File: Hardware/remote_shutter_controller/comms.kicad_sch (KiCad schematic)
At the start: 9 parts

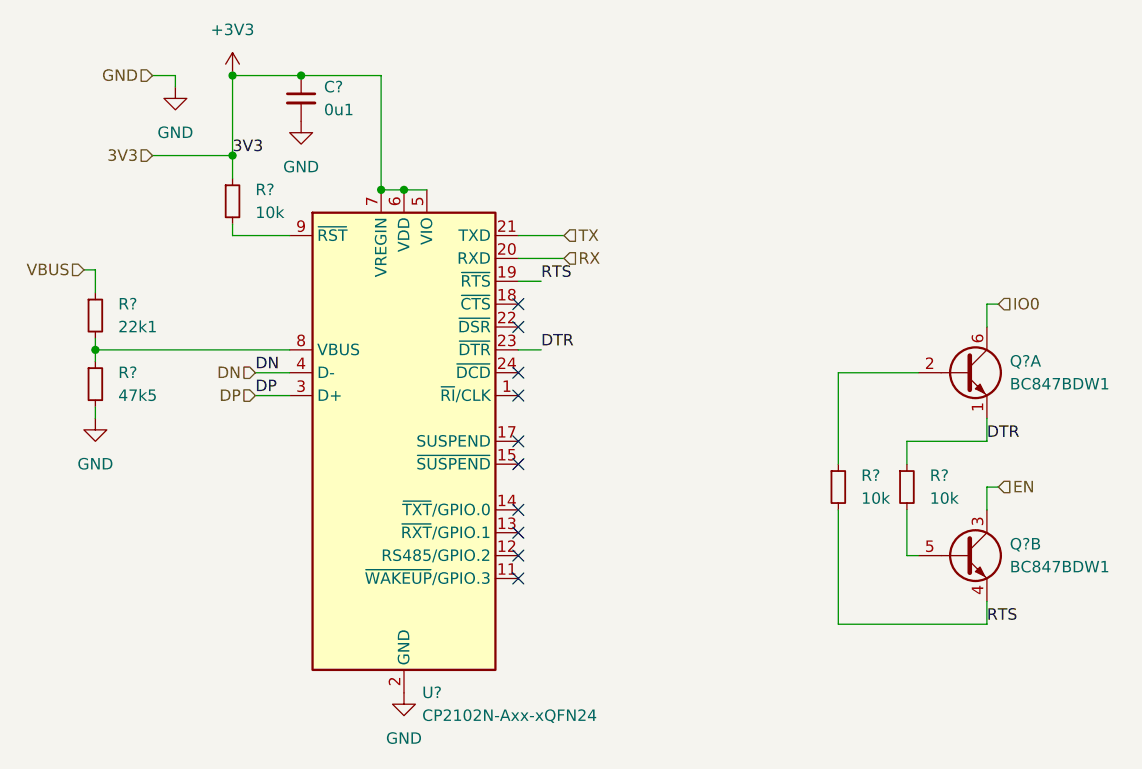
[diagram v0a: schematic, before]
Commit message: Schematic updates. First export to PCB
Added 9V line, OLED switch circuit. Added OLED footprint.
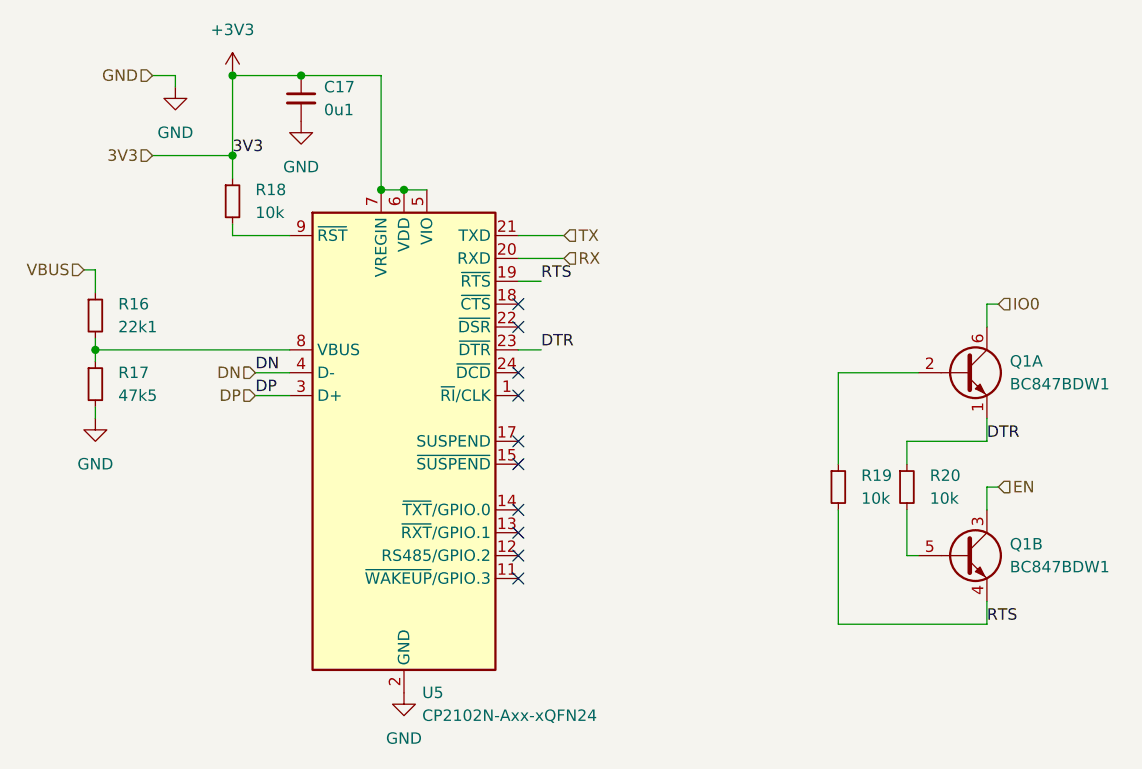
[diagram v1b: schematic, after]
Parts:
- gave numbers to parts that had none: 8
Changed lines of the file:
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@@
   (symbol (lib_id "power:GND") (at 95.25 97.79 0) (unit 1)
     (in_bom yes) (on_board yes) (fields_autoplaced)
-    (property "Reference" "#PWR?" (id 0) (at 95.25 104.14 0)
+    (property "Reference" "#PWR033" (id 0) (at 95.25 104.14 0)
       (effects (font (size 1.27 1.27)) hide)
     )
@@
   (symbol (lib_id "Device:R_Small") (at 95.25 86.36 0) (unit 1)
     (in_bom yes) (on_board yes) (fields_autoplaced)
-    (property "Reference" "R?" (id 0) (at 97.79 85.0899 0)
+    (property "Reference" "R16" (id 0) (at 97.79 85.0899 0)
       (effects (font (size 1.27 1.27)) (justify left))
     )
@@
   (symbol (lib_id "power:GND") (at 104.14 60.96 0) (unit 1)
     (in_bom yes) (on_board yes) (fields_autoplaced)
-    (property "Reference" "#PWR?" (id 0) (at 104.14 67.31 0)
+    (property "Reference" "#PWR034" (id 0) (at 104.14 67.31 0)
       (effects (font (size 1.27 1.27)) hide)
     )
@@
   (symbol (lib_id "power:+3V3") (at 110.49 59.69 0) (unit 1)
     (in_bom yes) (on_board yes) (fields_autoplaced)
-    (property "Reference" "#PWR?" (id 0) (at 110.49 63.5 0)
+    (property "Reference" "#PWR035" (id 0) (at 110.49 63.5 0)
       (effects (font (size 1.27 1.27)) hide)
     )
@@
   (symbol (lib_id "power:GND") (at 118.11 64.77 0) (unit 1)
     (in_bom yes) (on_board yes) (fields_autoplaced)
-    (property "Reference" "#PWR?" (id 0) (at 118.11 71.12 0)
+    (property "Reference" "#PWR036" (id 0) (at 118.11 71.12 0)
       (effects (font (size 1.27 1.27)) hide)
     )
@@
   (symbol (lib_id "Device:R_Small") (at 95.25 93.98 0) (unit 1)
     (in_bom yes) (on_board yes) (fields_autoplaced)
-    (property "Reference" "R?" (id 0) (at 97.79 92.7099 0)
+    (property "Reference" "R17" (id 0) (at 97.79 92.7099 0)
       (effects (font (size 1.27 1.27)) (justify left))
     )
@@
   (symbol (lib_id "Device:R_Small") (at 110.49 73.66 0) (unit 1)
     (in_bom yes) (on_board yes) (fields_autoplaced)
-    (property "Reference" "R?" (id 0) (at 113.03 72.3899 0)
+    (property "Reference" "R18" (id 0) (at 113.03 72.3899 0)
       (effects (font (size 1.27 1.27)) (justify left))
     )
@@
   (symbol (lib_id "Interface_USB:CP2102N-Axx-xQFN24") (at 129.54 100.33 0) (unit 1)
     (in_bom yes) (on_board yes) (fields_autoplaced)
-    (property "Reference" "U?" (id 0) (at 131.5594 128.27 0)
+    (property "Reference" "U5" (id 0) (at 131.5594 128.27 0)
       (effects (font (size 1.27 1.27)) (justify left))
     )
@@
   (symbol (lib_id "Device:R_Small") (at 177.8 105.41 0) (unit 1)
     (in_bom yes) (on_board yes) (fields_autoplaced)
-    (property "Reference" "R?" (id 0) (at 180.34 104.1399 0)
+    (property "Reference" "R19" (id 0) (at 180.34 104.1399 0)
       (effects (font (size 1.27 1.27)) (justify left))
     )
@@
   (symbol (lib_id "Transistor_BJT:BC847BDW1") (at 191.77 92.71 0) (unit 1)
     (in_bom yes) (on_board yes) (fields_autoplaced)
-    (property "Reference" "Q?" (id 0) (at 196.85 91.4399 0)
+    (property "Reference" "Q1" (id 0) (at 196.85 91.4399 0)
       (effects (font (size 1.27 1.27)) (justify left))
     )
@@
   (symbol (lib_id "Device:R_Small") (at 185.42 105.41 0) (unit 1)
     (in_bom yes) (on_board yes) (fields_autoplaced)
-    (property "Reference" "R?" (id 0) (at 187.96 104.1399 0)
+    (property "Reference" "R20" (id 0) (at 187.96 104.1399 0)
       (effects (font (size 1.27 1.27)) (justify left))
     )
@@
   (symbol (lib_id "Transistor_BJT:BC847BDW1") (at 191.77 113.03 0) (unit 2)
     (in_bom yes) (on_board yes) (fields_autoplaced)
-    (property "Reference" "Q?" (id 0) (at 196.85 111.7599 0)
+    (property "Reference" "Q1" (id 0) (at 196.85 111.7599 0)
       (effects (font (size 1.27 1.27)) (justify left))
     )
@@
   (symbol (lib_id "power:GND") (at 129.54 128.27 0) (unit 1)
     (in_bom yes) (on_board yes) (fields_autoplaced)
-    (property "Reference" "#PWR?" (id 0) (at 129.54 134.62 0)
+    (property "Reference" "#PWR037" (id 0) (at 129.54 134.62 0)
       (effects (font (size 1.27 1.27)) hide)
     )
@@
   (symbol (lib_id "Device:C_Small") (at 118.11 62.23 0) (unit 1)
     (in_bom yes) (on_board yes) (fields_autoplaced)
-    (property "Reference" "C?" (id 0) (at 120.65 60.9662 0)
-      (effects (font (size 1.27 1.27)) (justify left))
-    )
+    (property "Reference" "C17" (id 0) (at 120.65 60.9662 0)
+      (effects (font (size 1.27 1.27)) (justify left))
+    )
